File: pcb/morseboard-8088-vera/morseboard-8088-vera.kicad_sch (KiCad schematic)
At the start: 60 parts, among them J1 USB_B, J2 UART1, SW1 SW_SPDT, SW2 INTPORT, SW4 NMI, SW6 RESET, U1 8088, U10 74HCT273, U11 TL16C550, U12 74HC245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

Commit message: Initial commit VERA daughterboard
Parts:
- added J3: Bus, veraboard:veraboard, symbol Connector_Generic:Conn_02x12_Odd_Even
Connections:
- net A0: now also J3.19 (Pin_19)
- net A1: now also J3.20 (Pin_20)
- net A2: now also J3.17 (Pin_17)
- net A3: now also J3.18 (Pin_18)
- net A4: now also J3.15 (Pin_15)
- net D0: now also J3.10 (Pin_10)
- net D1: now also J3.9 (Pin_9)
- net D2: now also J3.8 (Pin_8)
- net D3: now also J3.7 (Pin_7)
- net D4: now also J3.6 (Pin_6)
- net D5: now also J3.5 (Pin_5)
- net D6: now also J3.4 (Pin_4)
- net D7: now also J3.3 (Pin_3)
- net GND: now also J3.2 (Pin_2), J3.21 (Pin_21)
- net VCC: now also J3.1 (Pin_1)
- net ~{RD}: now also J3.16 (Pin_16)
- net ~{RES}: now also J3.12 (Pin_12)
- net ~{WR}: now also J3.13 (Pin_13)
- net ~{IO02}: now reaches U6.13 (~{Y2})
- net ~{IO02}: now also J3.11 (Pin_11)
- no-connect marks 32 -> 34
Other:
- note added: "0x40"
- moved on the sheet: C16, C17, C18, C19, C20, C21, U11, U13

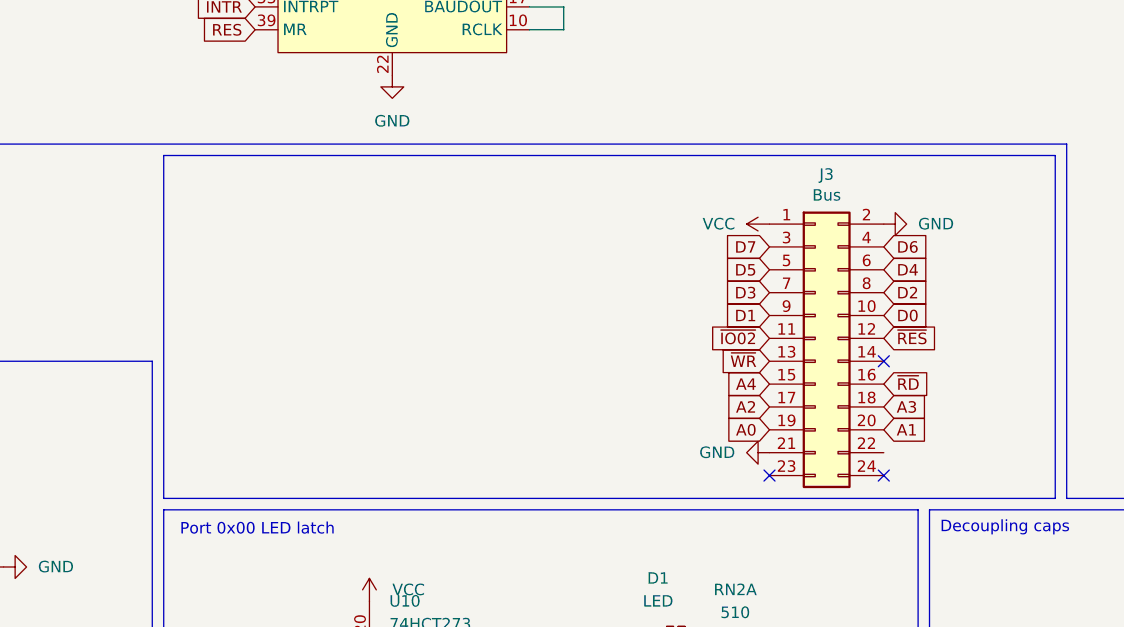
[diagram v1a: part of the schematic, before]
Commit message: Further shaping board
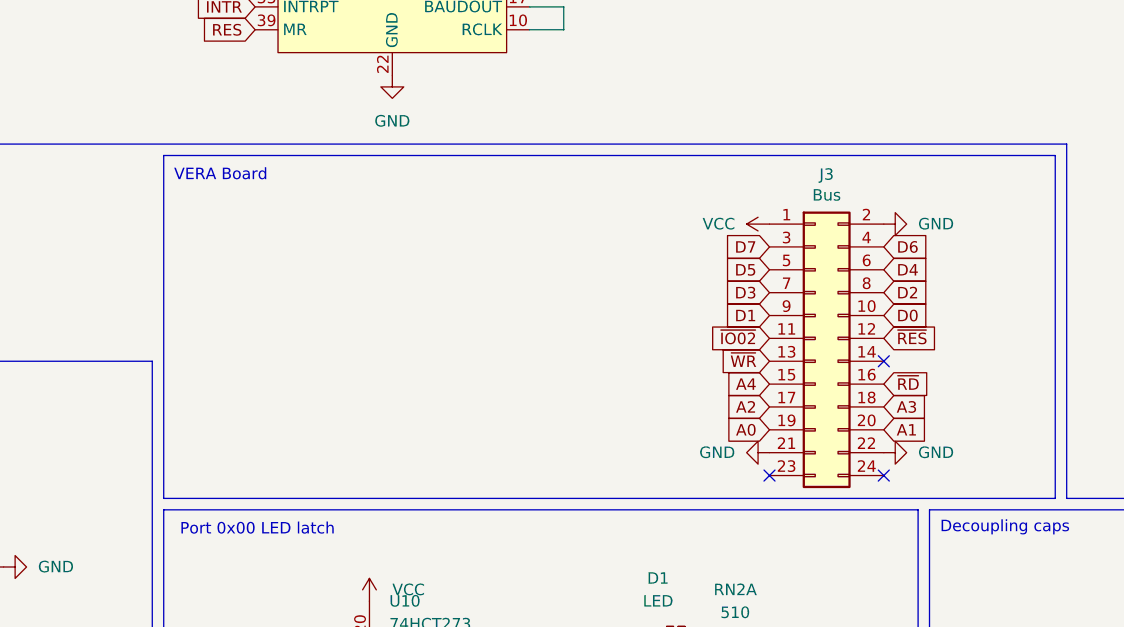
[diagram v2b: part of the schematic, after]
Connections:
- net GND: now also J3.22 (Pin_22)
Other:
- note added: "VERA Board"
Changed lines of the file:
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@@
 		)
 	)
+	(text "VERA Board"
+		(exclude_from_sim no)
+		(at 262.89 108.966 0)
+		(effects
+			(font
+				(size 1.27 1.27)
+			)
+		)
+	)
 	(text "Glue logic"
 		(exclude_from_sim no)
@@
 				)
 			)
+		)
+	)
+	(symbol
+		(lib_id "power:GND")
+		(at 336.55 139.7 90)
+		(unit 1)
+		(body_style 1)
+		(exclude_from_sim no)
+		(in_bom yes)
+		(on_board yes)
+		(in_pos_files yes)
+		(dnp no)
+		(fields_autoplaced yes)
+		(property "Reference" "#PWR0106"
+			(at 342.9 139.7 0)
+			(hide yes)
+			(show_name no)
+			(do_not_autoplace no)
+			(effects
+				(font
+					(size 1.27 1.27)
+				)
+			)
+		)
+		(property "Value" "GND"
+			(at 340.36 139.6999 90)
+			(show_name no)
+			(do_not_autoplace no)
+			(effects
+				(font
+					(size 1.27 1.27)
+				)
+				(justify right)
+			)
+		)
+		(property "Footprint" ""
+			(at 336.55 139.7 0)
+			(hide yes)
+			(show_name no)
+			(do_not_autoplace no)
+			(effects
+				(font
+					(size 1.27 1.27)
+				)
+			)
+		)
+		(property "Datasheet" ""
+			(at 336.55 139.7 0)
+			(hide yes)
+			(show_name no)
+			(do_not_autoplace no)
+			(effects
+				(font
+					(size 1.27 1.27)
+				)
+			)
+		)
+		(property "Description" "Power symbol creates a global label with name \"GND\" , ground"
+			(at 336.55 139.7 0)
+			(hide yes)
+			(show_name no)
+			(do_not_autoplace no)
+			(effects
+				(font
+					(size 1.27 1.27)
+				)
+			)
+		)
+		(pin "1"
+		)
+		(instances
+			(project "morseboard-8088-vera"
+				(path "/27cb38f9-12de-466e-a080-2dfa091752ed"
+					(reference "#PWR0106")
+					(unit 1)
+				)
+			)

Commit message: Building VERA prototype
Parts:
- removed C10: 100nF, Capacitor_THT:C_Disc_D5.0mm_W2.5mm_P5.00mm, symbol Device:C
- removed RN1: 10k, Resistor_THT:R_Array_SIP9, symbol Device:R_Network08
- removed SW2: INTPORT, Button_Switch_THT:SW_DIP_SPSTx08_Slide_9.78x22.5mm_W7.62mm_P2.54mm, symbol Switch:SW_DIP_x08
- removed SW6: RESET, Button_Switch_THT:SW_PUSH_6mm, symbol Switch:SW_Push
- removed U12: 74HC245, Package_DIP:DIP-20_W7.62mm_Socket, symbol 74xx:74HC245
- removed U14: DS1813, Package_TO_SOT_THT:TO-92, symbol Connector:Conn_01x03_Pin
- removed unit 3 of U7
- removed unit 4 of U7
- U5: footprint Socket:DIP_Socket-32_W11.9_W12.7_W15.24_W17.78_W18.5_3M_232-1285-00-0602J -> Socket:DIP_Socket-32_W11.9mm_W12.7mm_W15.24mm_W17.78mm_W18.5mm_3M_232-1285-00-0602J
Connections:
- net INTR: no longer U11.33 (INTRPT)
- net ~{IO03}: now reaches U6.12 (~{Y3})
- net VERA_INT: now reaches J3.14 (Pin_14)
- new net SERIAL_INT: U11.33 (INTRPT)
- no-connect marks 34 -> 30
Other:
- added sheet controller (controller.kicad_sch)
- note added: "0x00: LED"
- note added: "0x20: SERIAL"
- note added: "0x40: VERA"
- note added: "0x60: KB"
- note removed: "0x00"
- note removed: "0x20"
- note removed: "0x40"
- note removed: "DIP switch interrupt vector"
- moved on the sheet: C1, C14, C2, J1, R1, R8, SW4
